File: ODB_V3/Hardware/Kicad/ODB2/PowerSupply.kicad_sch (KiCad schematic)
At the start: 53 parts, among them U13 L6981N33DR, U7 MPQ9843GLE-5-AEC1-Z

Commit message: chore: update some footprint
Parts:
- removed Vin_C4: 100uF, symbol Device:C_Polarized_Small_US
- added Vin_C4: 100uf, ODB:WCAP-PSHP_8X8.7_DXL_, symbol ODB2:875115652007
- NT1, NT2, NT3, NT4: footprint (none) -> NetTie:NetTie-2_SMD_Pad0.5mm
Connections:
- net GND: now also Vin_C4.2
- net Vin: now also Vin_C4.1
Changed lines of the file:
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@@
 			)
 		)
-		(property "Footprint" ""
+		(property "Footprint" "NetTie:NetTie-2_SMD_Pad0.5mm"
 			(at 110.49 181.61 0)
 			(effects
@@
 	)
 	(symbol
-		(lib_id "Device:C_Polarized_Small_US")
-		(at 21.59 38.1 0)
-		(unit 1)
-		(exclude_from_sim no)
-		(in_bom yes)
-		(on_board yes)
-		(dnp no)
-		(property "Reference" "Vin_C4"
-			(at 21.844 36.322 0)
-			(effects
-				(font
-					(size 1.27 1.27)
-				)
-				(justify left)
-			)
-		)
-		(property "Value" "100uF"
-			(at 22.098 39.878 0)
-			(effects
-				(font
-					(size 1.27 1.27)
-				)
-				(justify left)
-			)
-		)
-		(property "Footprint" ""
-			(at 21.59 38.1 0)
-			(effects
-				(font
-					(size 1.27 1.27)
-				)
-				(hide yes)
-			)
-		)
-		(property "Datasheet" "~"
-			(at 21.59 38.1 0)
-			(effects
-				(font
-					(size 1.27 1.27)
-				)
-				(hide yes)
-			)
-		)
-		(property "Description" "Polarized capacitor, small US symbol"
-			(at 21.59 38.1 0)
-			(effects
-				(font
-					(size 1.27 1.27)
-				)
-				(hide yes)
-			)
-		)
-		(pin "1"
-		)
-		(pin "2"
-		)
-		(instances
-			(project ""
-				(path "/4b06c5d1-aa8b-48ed-8972-b43a60cfab78/a0dfa29e-ccca-4096-8481-c7e33c67aac5"
-					(reference "Vin_C4")
-					(unit 1)
-				)
-			)
-		)
-	)
-	(symbol
 		(lib_id "power:GND")
 		(at 265.43 33.02 0)
@@
 	)
 	(symbol
+		(lib_id "ODB2:875115652007")
+		(at 21.59 38.1 0)
+		(unit 1)
+		(exclude_from_sim no)
+		(in_bom yes)
+		(on_board yes)
+		(dnp no)
+		(property "Reference" "Vin_C4"
+			(at 25.146 35.814 0)
+			(effects
+				(font
+					(size 1.27 1.27)
+				)
+			)
+		)
+		(property "Value" "100uf"
+			(at 21.844 40.132 0)
+			(effects
+				(font
+					(size 1.27 1.27)
+				)
+				(justify left)
+			)
+		)
+		(property "Footprint" "ODB:WCAP-PSHP_8X8.7_DXL_"
+			(at 21.59 38.1 0)
+			(effects
+				(font
+					(size 1.27 1.27)
+				)
+				(hide yes)
+			)
+		)
+		(property "Datasheet" "https://www.digikey.ca/en/products/detail/w%C3%BCrth-elektronik/875115652007/8556615"
+			(at 21.59 38.1 0)
+			(effects
+				(font
+					(size 1.27 1.27)
+				)
+				(hide yes)
+			)
+		)
+		(property "Description" "CAP ALUM POLY 100UF 20% 35V SMD"
+			(at 21.59 38.1 0)
+			(effects
+				(font
+					(size 1.27 1.27)
+				)
+				(hide yes)
+			)
+		)
+		(pin "1"
+		)
+		(pin "2"
+		)
+		(instances
+			(project ""
+				(path "/4b06c5d1-aa8b-48ed-8972-b43a60cfab78/a0dfa29e-ccca-4096-8481-c7e33c67aac5"
+					(reference "Vin_C4")
+					(unit 1)
+				)
+			)
+		)
+	)
+	(symbol
 		(lib_id "power:GND")
 		(at 50.8 80.01 0)
@@
 			)
 		)
-		(property "Footprint" ""
+		(property "Footprint" "NetTie:NetTie-2_SMD_Pad0.5mm"
 			(at 110.49 186.69 0)
 			(effects
@@
 			)
 		)
-		(property "Footprint" ""
+		(property "Footprint" "NetTie:NetTie-2_SMD_Pad0.5mm"
 			(at 144.78 101.6 0)
 			(effects
@@
 			)
 		)
-		(property "Footprint" ""
+		(property "Footprint" "NetTie:NetTie-2_SMD_Pad0.5mm"
 			(at 144.78 107.95 0)
 			(effects

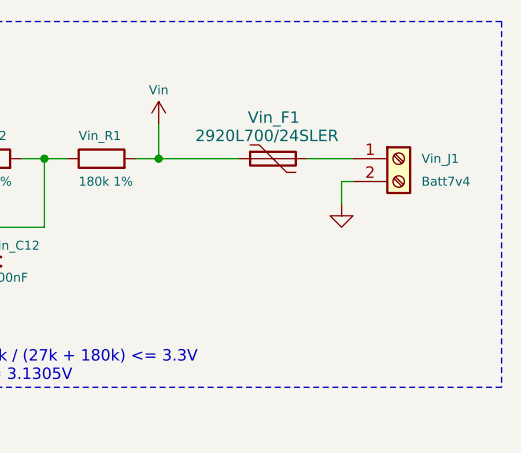
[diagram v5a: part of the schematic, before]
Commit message: feat: add xt30 footprint + GT17HN-4DP-2H and make component groups
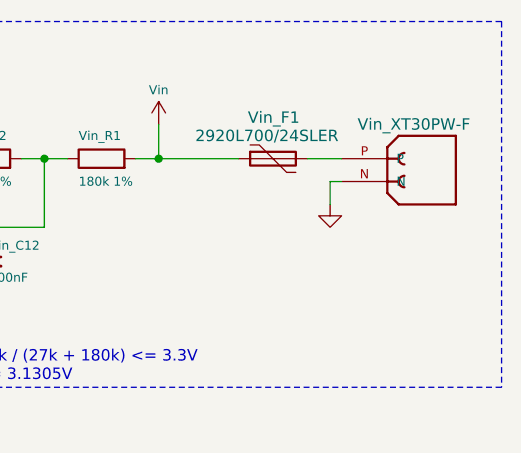
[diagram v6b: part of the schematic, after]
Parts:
- removed Vin_J1: Batt7v4, Connector_Wire:SolderWire-2.5sqmm_1x02_P8.8mm_D2.4mm_OD4.4mm, symbol Connector:Screw_Terminal_01x02
- added J15: Vin_XT30PW-F, ODB:AMASS_XT30PW-F, symbol ODB2:XT30PW-F
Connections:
- net GND: now also J15.N
- net at Vin_F1.2: now also J15.P
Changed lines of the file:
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@@
 	(wire
 		(pts
-			(xy 265.43 30.48) (xy 265.43 33.02)
+			(xy 264.16 30.48) (xy 264.16 33.02)
 		)
 		(stroke
@@
 	(wire
 		(pts
-			(xy 266.7 30.48) (xy 265.43 30.48)
-		)
-		(stroke
-			(width 0)
-			(type default)
-		)
-	)
-	(wire
-		(pts
 			(xy 142.24 83.82) (xy 143.51 83.82)
 		)
@@
 	(wire
 		(pts
-			(xy 261.62 27.94) (xy 266.7 27.94)
+			(xy 261.62 27.94) (xy 265.43 27.94)
 		)
 		(stroke
@@
 	(wire
 		(pts
+			(xy 264.16 30.48) (xy 265.43 30.48)
+		)
+		(stroke
+			(width 0)
+			(type default)
+		)
+	)
+	(wire
+		(pts
 			(xy 113.03 181.61) (xy 114.3 181.61)
 		)
@@
 	(symbol
 		(lib_id "power:GND")
-		(at 265.43 33.02 0)
+		(at 264.16 33.02 0)
 		(unit 1)
 		(exclude_from_sim no)
@@
 		(fields_autoplaced yes)
 		(property "Reference" "#PWR032"
-			(at 265.43 39.37 0)
+			(at 264.16 39.37 0)
 			(effects
 				(font
@@
 		)
 		(property "Value" "GND"
-			(at 265.43 38.1 0)
+			(at 264.16 38.1 0)
 			(effects
 				(font
@@
 		)
 		(property "Footprint" ""
-			(at 265.43 33.02 0)
+			(at 264.16 33.02 0)
 			(effects
 				(font
@@
 		)
 		(property "Datasheet" ""
-			(at 265.43 33.02 0)
+			(at 264.16 33.02 0)
 			(effects
 				(font
@@
 		)
 		(property "Description" ""
-			(at 265.43 33.02 0)
+			(at 264.16 33.02 0)
 			(effects
 				(font
@@
 	)
 	(symbol
-		(lib_id "Connector:Screw_Terminal_01x02")
-		(at 271.78 27.94 0)
-		(unit 1)
-		(exclude_from_sim no)
-		(in_bom yes)
-		(on_board yes)
-		(dnp no)
-		(fields_autoplaced yes)
-		(property "Reference" "Vin_J1"
-			(at 274.32 27.94 0)
-			(effects
-				(font
-					(size 1 1)
-				)
-				(justify left)
-			)
-		)
-		(property "Value" "Batt7v4"
-			(at 274.32 30.48 0)
-			(effects
-				(font
-					(size 1 1)
-				)
-				(justify left)
-			)
-		)
-		(property "Footprint" "Connector_Wire:SolderWire-2.5sqmm_1x02_P8.8mm_D2.4mm_OD4.4mm"
-			(at 271.78 27.94 0)
-			(effects
-				(font
-					(size 1 1)
-				)
-				(hide yes)
-			)
-		)
-		(property "Datasheet" "~"
-			(at 271.78 27.94 0)
-			(effects
-				(font
-					(size 1 1)
-				)
-				(hide yes)
-			)
-		)
-		(property "Description" ""
-			(at 271.78 27.94 0)
-			(effects
-				(font
-					(size 1.27 1.27)
-				)
-				(hide yes)
-			)
-		)
-		(pin "1"
-		)
-		(pin "2"
-		)
-		(instances
-			(project "ODB2"
-				(path "/4b06c5d1-aa8b-48ed-8972-b43a60cfab78/a0dfa29e-ccca-4096-8481-c7e33c67aac5"
-					(reference "Vin_J1")
-					(unit 1)
-				)
-			)
-		)
-	)
-	(symbol
 		(lib_id "power:+5V")
 		(at 60.96 102.87 0)
@@
 					(unit 1)
 				)
+			)
+		)
+	)
+	(symbol
+		(lib_id "ODB2:XT30PW-F")
+		(at 270.51 27.94 0)
+		(mirror y)
+		(unit 1)
+		(exclude_from_sim no)
+		(in_bom yes)
+		(on_board yes)
+		(dnp no)
+		(property "Reference" "J15"
+			(at 279.4 27.9399 0)
+			(effects
+				(font
+					(size 1.27 1.27)
+				)
+				(justify right)
+				(hide yes)
+			)
+		)
+		(property "Value" "Vin_XT30PW-F"
+			(at 267.208 24.13 0)
+			(effects
+				(font
+					(size 1.27 1.27)
+				)
+				(justify right)
+			)
+		)
+		(property "Footprint" "ODB:AMASS_XT30PW-F"
+			(at 270.51 27.94 0)
+			(effects
+				(font
+					(size 1.27 1.27)
+				)
+				(justify bottom)
+				(hide yes)
+			)
+		)
+		(property "Datasheet" ""
+			(at 270.51 27.94 0)
+			(effects
+				(font
+					(size 1.27 1.27)
+				)
+				(hide yes)
+			)
+		)
+		(property "Description" ""
+			(at 270.51 27.94 0)
+			(effects
+				(font
+					(size 1.27 1.27)
+				)
+				(hide yes)
+			)
+		)
+		(property "MF" "amass"
+			(at 270.51 27.94 0)
+			(effects
+				(font
+					(size 1.27 1.27)
+				)
+				(justify bottom)
+				(hide yes)
+			)
+		)
+		(property "MAXIMUM_PACKAGE_HEIGHT" "5 mm"
+			(at 270.51 27.94 0)
+			(effects
+				(font
+					(size 1.27 1.27)
+				)
+				(justify bottom)
+				(hide yes)
+			)
+		)
+		(property "Package" "None"
+			(at 270.51 27.94 0)
+			(effects
+				(font
+					(size 1.27 1.27)
+				)
+				(justify bottom)
+				(hide yes)
+			)
+		)
+		(property "Price" "None"
+			(at 270.51 27.94 0)
+			(effects
+				(font
+					(size 1.27 1.27)
+				)
+				(justify bottom)
+				(hide yes)
+			)
+		)
+		(property "Check_prices" "https://www.snapeda.com/parts/XT30PW-F/AMASS/view-part/?ref=eda"
+			(at 270.51 27.94 0)
+			(effects
+				(font
+					(size 1.27 1.27)
+				)
+				(justify bottom)
+				(hide yes)
+			)
+		)
+		(property "STANDARD" "Manufacturer Recommendations"
+			(at 270.51 27.94 0)
+			(effects
+				(font
+					(size 1.27 1.27)
+				)
+				(justify bottom)
+				(hide yes)
+			)
+		)
+		(property "PARTREV" "1.2"
+			(at 270.51 27.94 0)
+			(effects
+				(font
+					(size 1.27 1.27)
+				)
+				(justify bottom)
+				(hide yes)
+			)
+		)
+		(property "SnapEDA_Link" "https://www.snapeda.com/parts/XT30PW-F/AMASS/view-part/?ref=snap"
+			(at 270.51 27.94 0)
+			(effects
+				(font
+					(size 1.27 1.27)
+				)
+				(justify bottom)
+				(hide yes)
+			)
+		)
+		(property "MP" "XT30PW-F"
+			(at 270.51 27.94 0)
+			(effects
+				(font
+					(size 1.27 1.27)
+				)
+				(justify bottom)
+				(hide yes)
+			)
+		)
+		(property "Description_1" "Socket; DC supply; XT30; female; PIN: 2; on PCBs; THT; yellow; 15A"
+			(at 270.51 27.94 0)
+			(effects
+				(font
+					(size 1.27 1.27)
+				)
+				(justify bottom)
+				(hide yes)
+			)
+		)
+		(property "MANUFACTURER" "Amass"
+			(at 270.51 27.94 0)
+			(effects
+				(font
+					(size 1.27 1.27)
+				)
+				(justify bottom)
+				(hide yes)
+			)
+		)
+		(property "Availability" "In Stock"
+			(at 270.51 27.94 0)
+			(effects
+				(font
+					(size 1.27 1.27)
+				)
+				(justify bottom)
+				(hide yes)
+			)
+		)
+		(property "SNAPEDA_PN" "XT30PW-F"
+			(at 270.51 27.94 0)
+			(effects
+				(font
+					(size 1.27 1.27)
+				)
+				(justify bottom)
+				(hide yes)
+			)
+		)
+		(pin "P"
+		)
+		(pin "N"
+		)
+		(instances
+			(project ""
+				(path "/4b06c5d1-aa8b-48ed-8972-b43a60cfab78/a0dfa29e-ccca-4096-8481-c7e33c67aac5"
+					(reference "J15")
+					(unit 1)
+				)

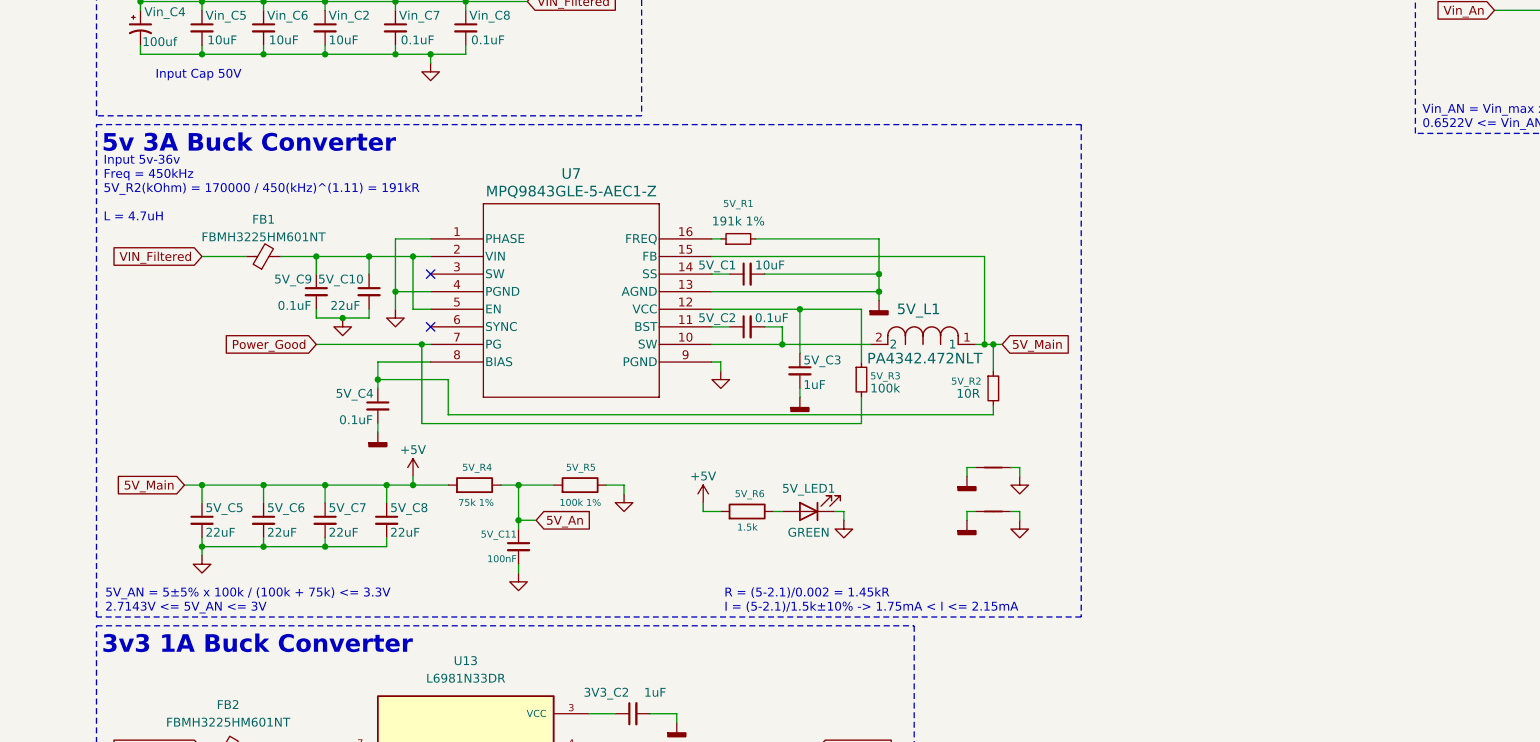
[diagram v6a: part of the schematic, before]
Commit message: Layout local STM, layout et routing local Buck 5V
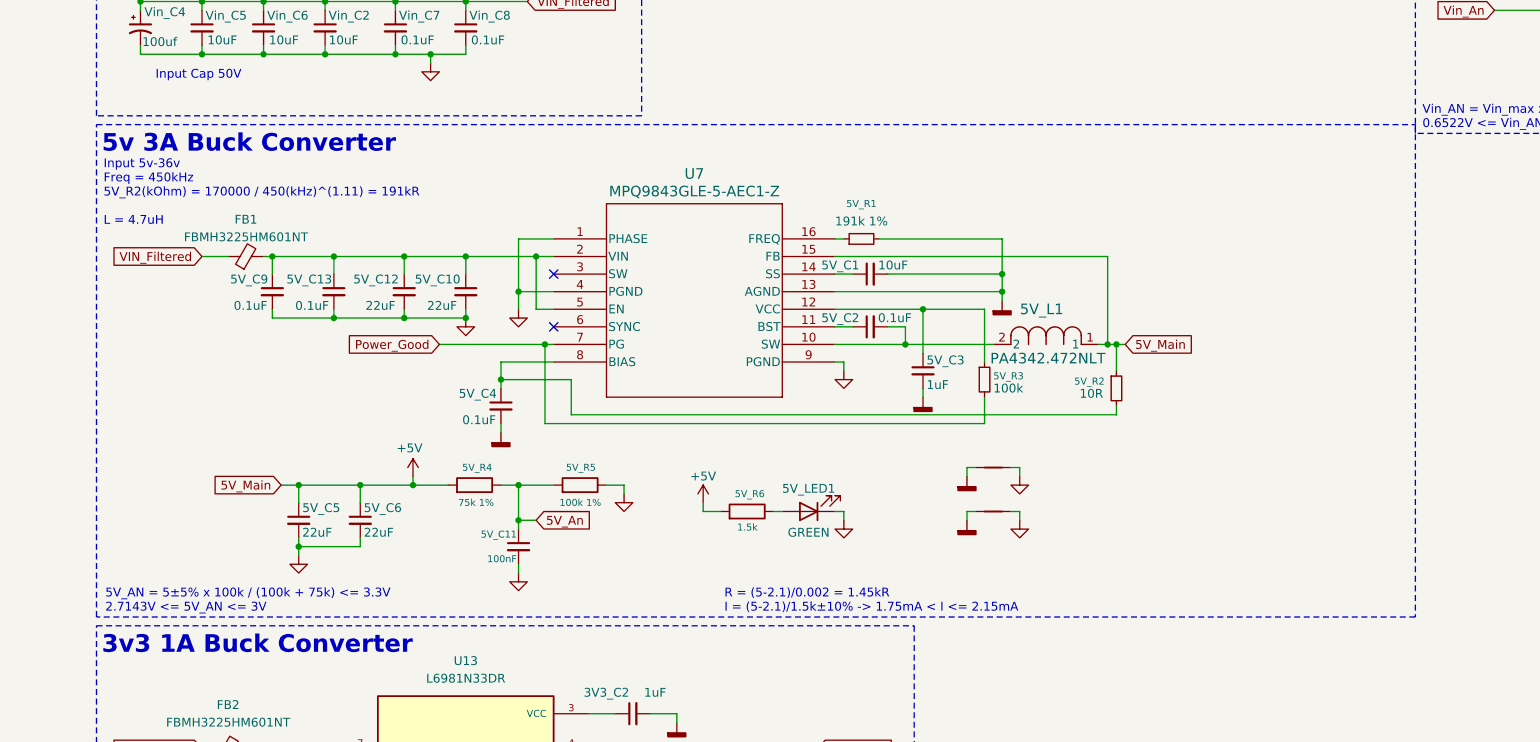
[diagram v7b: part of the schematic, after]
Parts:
- removed 5V_C7, 5V_C8: 22uF, Capacitor_SMD:C_1210_3225Metric, symbol Device:C_Small
- added 5V_C12: 22uF, Capacitor_SMD:C_1210_3225Metric, symbol Device:C_Small
- added 5V_C13: 0.1uF, Capacitor_SMD:C_0402_1005Metric, symbol Device:C_Small
- 5V_C10: footprint Capacitor_SMD:C_0603_1608Metric -> Capacitor_SMD:C_1210_3225Metric
- 5V_C2, 5V_C4, 5V_C9: footprint Capacitor_SMD:C_0603_1608Metric -> Capacitor_SMD:C_0402_1005Metric
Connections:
- net GND: now also 5V_C12.2, 5V_C13.2
- net at 5V_C10.1, 5V_C9.1, FB1.2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: now also 5V_C12.1, 5V_C13.1
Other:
- moved on the sheet: 5V_C1, 5V_C10, 5V_C2, 5V_C3, 5V_C4, 5V_C5, 5V_C6, 5V_C9, 5V_L1, 5V_R1, 5V_R2, 5V_R3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

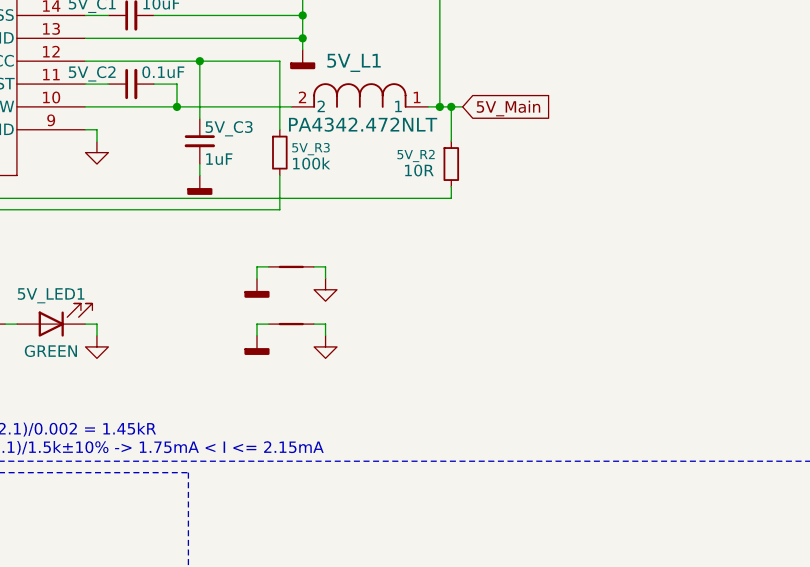
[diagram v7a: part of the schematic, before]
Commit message: fix : Buck 5V traces and powerplane isolation
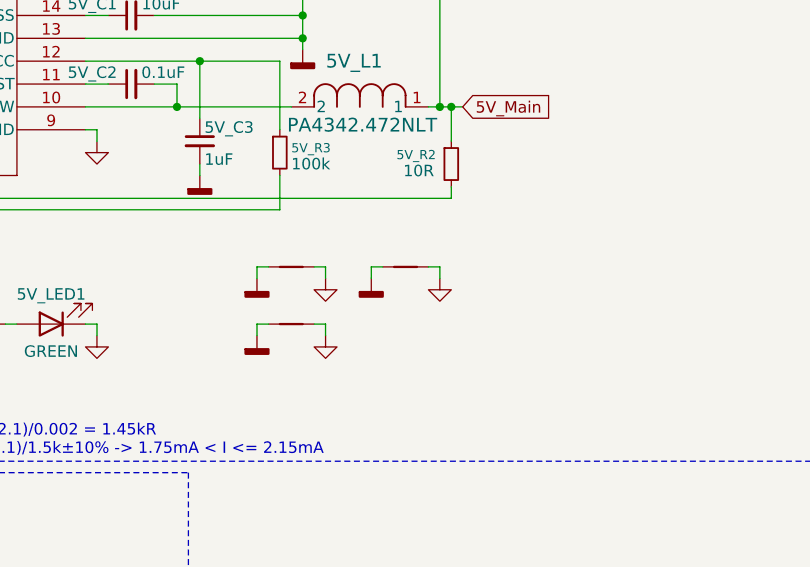
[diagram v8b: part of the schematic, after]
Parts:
- added NT5: NetTie_2, NetTie:NetTie-2_SMD_Pad0.5mm, symbol Device:NetTie_2
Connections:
- net AGND5V: now also NT5.1
- net GND: now also NT5.2
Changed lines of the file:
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@@
 	(wire
 		(pts
+			(xy 161.29 101.6) (xy 161.29 102.87)
+		)
+		(stroke
+			(width 0)
+			(type default)
+		)
+	)
+	(wire
+		(pts
 			(xy 81.28 78.74) (xy 78.74 78.74)
 		)
@@
 	(wire
 		(pts
+			(xy 160.02 101.6) (xy 161.29 101.6)
+		)
+		(stroke
+			(width 0)
+			(type default)
+		)
+	)
+	(wire
+		(pts
 			(xy 116.84 175.26) (xy 118.11 175.26)
 		)
@@
 	(wire
 		(pts
+			(xy 154.94 101.6) (xy 153.67 101.6)
+		)
+		(stroke
+			(width 0)
+			(type default)
+		)
+	)
+	(wire
+		(pts
 			(xy 49.53 80.01) (xy 40.64 80.01)
 		)
@@
 	(wire
 		(pts
+			(xy 153.67 101.6) (xy 153.67 102.87)
+		)
+		(stroke
+			(width 0)
+			(type default)
+		)
+	)
+	(wire
+		(pts
 			(xy 83.82 88.9) (xy 73.66 88.9)
 		)
@@
 	)
 	(symbol
+		(lib_id "power:GND")
+		(at 161.29 102.87 0)
+		(unit 1)
+		(exclude_from_sim no)
+		(in_bom yes)
+		(on_board yes)
+		(dnp no)
+		(fields_autoplaced yes)
+		(property "Reference" "#PWR0146"
+			(at 161.29 109.22 0)
+			(effects
+				(font
+					(size 1 1)
+				)
+				(hide yes)
+			)
+		)
+		(property "Value" "GND"
+			(at 161.29 107.95 0)
+			(effects
+				(font
+					(size 1 1)
+				)
+				(hide yes)
+			)
+		)
+		(property "Footprint" ""
+			(at 161.29 102.87 0)
+			(effects
+				(font
+					(size 1 1)
+				)
+				(hide yes)
+			)
+		)
+		(property "Datasheet" ""
+			(at 161.29 102.87 0)
+			(effects
+				(font
+					(size 1 1)
+				)
+				(hide yes)
+			)
+		)
+		(property "Description" ""
+			(at 161.29 102.87 0)
+			(effects
+				(font
+					(size 1.27 1.27)
+				)
+				(hide yes)
+			)
+		)
+		(pin "1"
+		)
+		(instances
+			(project "ODB2"
+				(path "/4b06c5d1-aa8b-48ed-8972-b43a60cfab78/a0dfa29e-ccca-4096-8481-c7e33c67aac5"
+					(reference "#PWR0146")
+					(unit 1)
+				)
+			)
+		)
+	)
+	(symbol
 		(lib_id "power:+5V")
 		(at 102.87 106.68 0)
@@
 	)
 	(symbol
+		(lib_id "power:GNDD")
+		(at 153.67 102.87 0)
+		(unit 1)
+		(exclude_from_sim no)
+		(in_bom yes)
+		(on_board yes)
+		(dnp no)
+		(fields_autoplaced yes)
+		(property "Reference" "#PWR0145"
+			(at 153.67 109.22 0)
+			(effects
+				(font
+					(size 1.27 1.27)
+				)
+				(hide yes)
+			)
+		)
+		(property "Value" "AGND5V"
+			(at 153.67 106.68 0)
+			(effects
+				(font
+					(size 1.27 1.27)
+				)
+				(hide yes)
+			)
+		)
+		(property "Footprint" ""
+			(at 153.67 102.87 0)
+			(effects
+				(font
+					(size 1.27 1.27)
+				)
+				(hide yes)
+			)
+		)
+		(property "Datasheet" ""
+			(at 153.67 102.87 0)
+			(effects
+				(font
+					(size 1.27 1.27)
+				)
+				(hide yes)
+			)
+		)
+		(property "Description" "Power symbol creates a global label with name \"GNDD\" , digital ground"
+			(at 153.67 102.87 0)
+			(effects
+				(font
+					(size 1.27 1.27)
+				)
+				(hide yes)
+			)
+		)
+		(pin "1"
+		)
+		(instances
+			(project "ODB2"
+				(path "/4b06c5d1-aa8b-48ed-8972-b43a60cfab78/a0dfa29e-ccca-4096-8481-c7e33c67aac5"
+					(reference "#PWR0145")
+					(unit 1)
+				)
+			)
+		)
+	)
+	(symbol
 		(lib_id "Device:C_Small")
 		(at 92.71 137.16 90)
@@
 					(unit 1)
 				)
+			)
+		)
+	)
+	(symbol
+		(lib_id "Device:NetTie_2")
+		(at 157.48 101.6 0)
+		(unit 1)
+		(exclude_from_sim no)
+		(in_bom no)
+		(on_board yes)
+		(dnp no)
+		(fields_autoplaced yes)
+		(property "Reference" "NT5"
+			(at 157.48 96.52 0)
+			(effects
+				(font
+					(size 1.27 1.27)
+				)
+				(hide yes)
+			)
+		)
+		(property "Value" "NetTie_2"
+			(at 157.48 99.06 0)
+			(effects
+				(font
+					(size 1.27 1.27)
+				)
+				(hide yes)
+			)
+		)
+		(property "Footprint" "NetTie:NetTie-2_SMD_Pad0.5mm"
+			(at 157.48 101.6 0)
+			(effects
+				(font
+					(size 1.27 1.27)
+				)
+				(hide yes)
+			)
+		)
+		(property "Datasheet" "~"
+			(at 157.48 101.6 0)
+			(effects
+				(font
+					(size 1.27 1.27)
+				)
+				(hide yes)
+			)
+		)
+		(property "Description" "Net tie, 2 pins"
+			(at 157.48 101.6 0)
+			(effects
+				(font
+					(size 1.27 1.27)
+				)
+				(hide yes)
+			)
+		)
+		(pin "2"
+		)
+		(pin "1"
+		)
+		(instances
+			(project "ODB2"
+				(path "/4b06c5d1-aa8b-48ed-8972-b43a60cfab78/a0dfa29e-ccca-4096-8481-c7e33c67aac5"
+					(reference "NT5")
+					(unit 1)
+				)
